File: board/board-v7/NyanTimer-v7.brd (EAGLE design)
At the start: 136.3 x 45 mm, 49 parts, among them IC1 7815DT, IC2 MAX232, IC3 7815DT, SW1 AKIZUKI_SWITCH, U1 328P

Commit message: modified
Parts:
- moved Q1 20.0 mm to (-49.0, -15.0)
- moved C14 10.0 mm to (-68.6, 16.4)
- moved C15 10.0 mm to (-63.5, 16.4)
- moved C12 10.0 mm to (-63.5, 20.2)
- moved C13 10.0 mm to (-68.6, 20.2)
- moved C16 10.0 mm to (-68.6, 12.5)
- moved IC2 10.0 mm to (-66.9, 32.5)
- moved BT1 5.00 mm to (-33.6, 25.8)
- moved BT2 5.00 mm to (33.6, 25.8)
- moved C4 5.00 mm to (-31.2, 21.2)
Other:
- board size 136.3 x 45 mm -> 136 x 45 mm

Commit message: modified
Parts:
- moved C13 139.0 mm to (70.4, 21.2)
- moved IC2 134.0 mm to (67.1, 33.5)
- moved C15 133.9 mm to (70.4, 17.1)
- moved C14 133.1 mm to (64.5, 17.1)
- moved C16 133.1 mm to (64.5, 13.1)
- moved C12 128.0 mm to (64.5, 21.2)
- moved C5 50.0 mm to (-23.0, 5.02)
- moved C6 50.0 mm to (-26.7, 5.04)
- moved PHN1 50.0 mm to (26.7, 2.14)
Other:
- outline, holes or cut-outs redrawn

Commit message: modified
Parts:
- moved C18 89.8 mm to (-1.00, 27.0)
- moved C17 77.6 mm to (-11.0, 27.0)
- moved R12 74.8 mm to (0.00, 20.0)
- moved Q1 63.0 mm to (-6.00, 31.0)
- moved C7 17.7 mm to (19.1, 22.4)
- moved PIN1 17.0 mm to (-30.7, 15.8)
- moved PIN2 17.0 mm to (30.8, 15.9)
- moved C1 12.0 mm to (-19.2, 15.6)
- moved C2 12.0 mm to (19.1, 15.6), turned to 270 degrees
- moved C4 12.0 mm to (-19.2, 21.2)
- moved R10 6.40 mm to (31.1, 8.83), turned to 270 degrees
- moved R11 6.40 mm to (-31.1, 8.84), turned to 270 degrees
- moved R2 5.00 mm to (2.55, 11.1)
- moved R1 5.00 mm to (-2.62, 11.1)
- moved R3 1.00 mm to (-11.4, 11.2)
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
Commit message: modified
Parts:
- C11, C9: value 0.1u -> 2.2u
- C8: value 200u -> 0.1u
- moved C17 12.9 mm to (1.75, 29.2), turned to 90 degrees
- moved R2 5.00 mm to (2.55, 16.1)
- moved R1 5.00 mm to (-2.62, 16.1)
- moved R12 4.00 mm to (0.00, 24.0)
- moved Q1 3.00 mm to (-9.00, 31.0)
- moved C18 2.26 mm to (-1.50, 29.2), turned to 90 degrees
- moved C8 1.50 mm to (5.01, 29.2)
- moved LED1 1.00 mm to (-17.4, 29.0)
- moved LED2 1.00 mm to (17.5, 28.9)
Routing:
- removed copper zone on layer 1, net GND

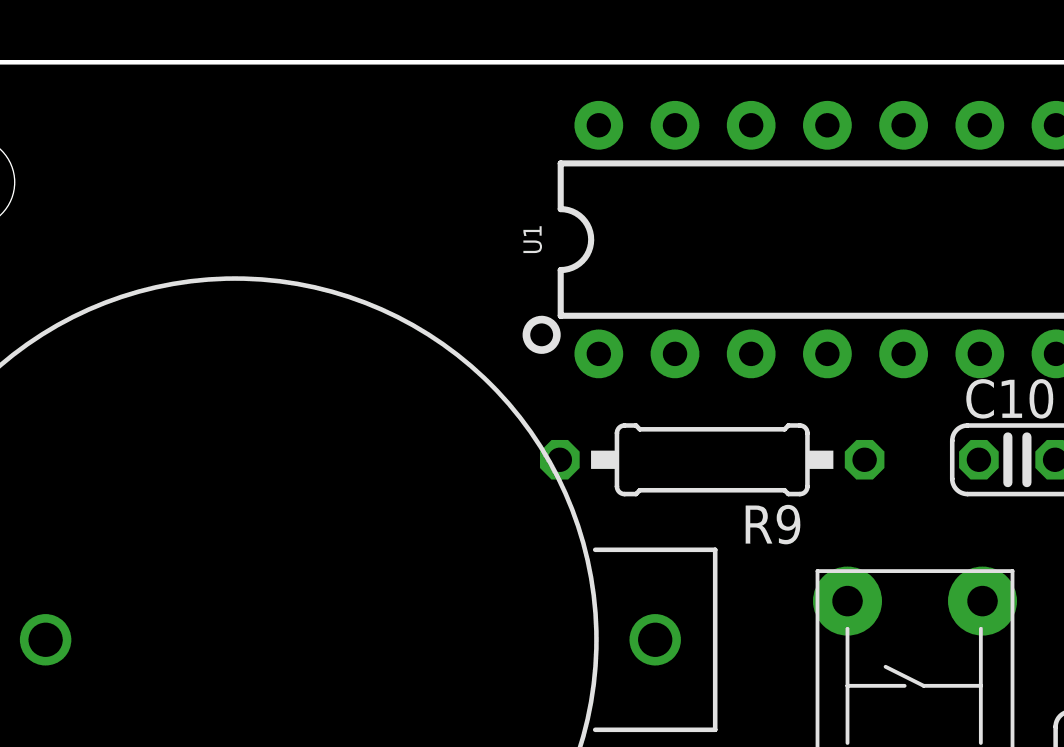
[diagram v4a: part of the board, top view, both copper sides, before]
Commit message: modified padl pin
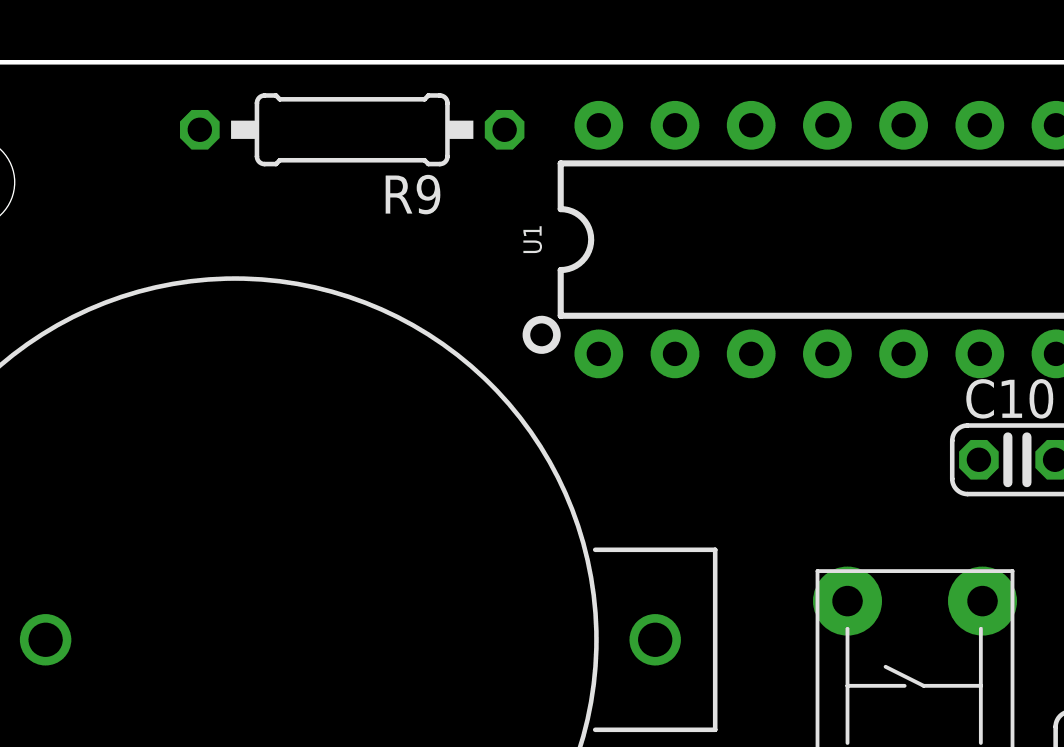
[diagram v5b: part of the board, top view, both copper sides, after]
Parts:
- moved R9 16.3 mm to (-43.8, 42.8)
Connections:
- net PADLIN: now also U1.25; no longer U1.11
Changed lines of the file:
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@@
 <drawing>
 <settings>
-<setting alwaysvectorfont="no"/>
+<setting alwaysvectorfont="yes"/>
 <setting verticaltext="up"/>
 </settings>
@@
 </layers>
 <board>
-<fusionsync huburn="a.cGVyc29uYWw6dWUyZDY1ODA3" projecturn="a.cGVyc29uYWw6dWUyZDY1ODA3IzIwMTgwOTMwMTUxNjc4Mzgx" f3durn="urn:adsk.wipprod:dm.lineage:cDSKwgNKRl2nwQcyNHv1MQ" pcbguid="a41a688f-10bb-486b-9802-a0f971612fa0" lastpulledtime="" lastsyncedchangeguid="592dcdca-8122-b4cd-fe00-eb67763abaf7"/>
+<fusionsync huburn="a.cGVyc29uYWw6dWUyZDY1ODA3" projecturn="a.cGVyc29uYWw6dWUyZDY1ODA3IzIwMTgwOTMwMTUxNjc4Mzgx" f3durn="urn:adsk.wipprod:dm.lineage:3ih9qoiSRh2YeH_9UNAHYQ" pcbguid="ba764a6a-c4ff-48dd-a9cc-70516c013fae" lastpulledtime="" lastsyncedchangeguid="48eea775-bd5d-98d6-e79d-8d9a8075f033"/>
 <plain>
 <hole x="-42" y="4" drill="3"/>
@@
 <element name="BT1" library="akizuki_cr2032" package="AKIZUKI_CR2032" value="AKIZUKI_CR2032" x="-33.65" y="25.75" smashed="yes" rot="R90"/>
 <element name="BT2" library="akizuki_cr2032" package="AKIZUKI_CR2032" value="AKIZUKI_CR2032" x="33.65" y="25.75" smashed="yes" rot="SR270"/>
-<element name="R9" library="resistor" library_urn="urn:adsk.eagle:library:348" package="0207/10" package3d_urn="urn:adsk.eagle:package:23491/2" value="10k" x="-31.75" y="31.75" smashed="yes" rot="R180">
-<attribute name="NAME" x="-28.702" y="30.226" size="1.27" layer="25" ratio="10" rot="R180"/>
-<attribute name="VALUE" x="-29.4894" y="32.385" size="1.27" layer="27" ratio="10" rot="R180"/>
+<element name="R9" library="resistor" library_urn="urn:adsk.eagle:library:348" package="0207/10" package3d_urn="urn:adsk.eagle:package:23491/2" value="10k" x="-43.75" y="42.75" smashed="yes" rot="R180">
+<attribute name="NAME" x="-40.702" y="41.226" size="1.27" layer="25" ratio="10" rot="R180"/>
+<attribute name="VALUE" x="-41.4894" y="43.385" size="1.27" layer="27" ratio="10" rot="R180"/>
 </element>
 <element name="IC2" library="maxim" library_urn="urn:adsk.eagle:library:269" package="DIL16" package3d_urn="urn:adsk.eagle:package:922/2" value="MAX232" x="67.11" y="33.47" smashed="yes" rot="R90">
@@
 <contactref element="C17" pad="2"/>
 <contactref element="C18" pad="2"/>
+<wire x1="53.97" y1="25.75" x2="63.3" y2="27.12" width="0" layer="19" extent="1-1"/>
+<wire x1="69.13" y1="17.15" x2="63.3" y2="27.12" width="0" layer="19" extent="1-1"/>
+<wire x1="65.79" y1="13.14" x2="69.13" y2="17.15" width="0" layer="19" extent="1-1"/>
+<wire x1="32.22" y1="37.16" x2="53.97" y2="25.75" width="0" layer="19" extent="1-1"/>
+<wire x1="17.74" y1="35.56" x2="32.22" y2="37.16" width="0" layer="19" extent="1-1"/>
+<wire x1="18.75" y1="28.91" x2="17.74" y2="35.56" width="0" layer="19" extent="1-1"/>
+<wire x1="11.16" y1="27.94" x2="18.75" y2="28.91" width="0" layer="19" extent="1-1"/>
+<wire x1="8.08" y1="27.9" x2="11.16" y2="27.94" width="0" layer="19" extent="1-1"/>
+<wire x1="5.01" y1="27.92" x2="8.08" y2="27.9" width="0" layer="19" extent="1-1"/>
+<wire x1="1.75" y1="30.47" x2="5.01" y2="27.92" width="0" layer="19" extent="1-1"/>
+<wire x1="-1.5" y1="30.47" x2="1.75" y2="30.47" width="0" layer="19" extent="1-1"/>
+<wire x1="19.14" y1="21.12" x2="18.75" y2="28.91" width="0" layer="19" extent="1-1"/>
+<wire x1="16.53" y1="17.2" x2="19.14" y2="21.12" width="0" layer="19" extent="1-1"/>
+<wire x1="16.53" y1="11.2" x2="16.53" y2="17.2" width="0" layer="19" extent="1-1"/>
+<wire x1="4.07" y1="40.45" x2="1.75" y2="30.47" width="0" layer="19" extent="1-1"/>
+<wire x1="26.69" y1="7.22" x2="16.53" y2="11.2" width="0" layer="19" extent="1-1"/>
+<wire x1="-6.37" y1="17.12" x2="-1.5" y2="30.47" width="0" layer="19" extent="1-1"/>
+<wire x1="-6.37" y1="11.2" x2="-6.37" y2="17.12" width="0" layer="19" extent="1-1"/>
+<wire x1="2.54" y1="2.97" x2="-6.37" y2="11.2" width="0" layer="19" extent="1-1"/>
+<wire x1="-17.75" y1="35.28" x2="-1.5" y2="30.47" width="0" layer="19" extent="1-1"/>
+<wire x1="-20.32" y1="31.75" x2="-17.75" y2="35.28" width="0" layer="19" extent="1-1"/>
+<wire x1="-18.67" y1="29.03" x2="-20.32" y2="31.75" width="0" layer="19" extent="1-1"/>
+<wire x1="-20.29" y1="42.9" x2="-17.75" y2="35.28" width="0" layer="19" extent="1-1"/>
 </signal>
 <signal name="+5V">
@@
 <wire x1="-20.29" y1="35.28" x2="-17.75" y2="42.9" width="0" layer="19" extent="1-1"/>
 <wire x1="-22.86" y1="31.75" x2="-20.29" y2="35.28" width="0" layer="19" extent="1-1"/>
-<wire x1="-26.67" y1="31.75" x2="-22.86" y2="31.75" width="0" layer="19" extent="1-1"/>
-<wire x1="-27.24" y1="27.04" x2="-26.67" y2="31.75" width="0" layer="19" extent="1-1"/>
+<wire x1="-27.24" y1="27.04" x2="-22.86" y2="31.75" width="0" layer="19" extent="1-1"/>
 <wire x1="-27.27" y1="17.98" x2="-27.24" y2="27.04" width="0" layer="19" extent="1-1"/>
 <wire x1="-19.16" y1="19.93" x2="-27.27" y2="17.98" width="0" layer="19" extent="1-1"/>
 <wire x1="-19.18" y1="14.34" x2="-19.16" y2="19.93" width="0" layer="19" extent="1-1"/>
+<wire x1="-38.67" y1="42.75" x2="-22.86" y2="31.75" width="0" layer="19" extent="1-1"/>
 </signal>
 <signal name="BUZ+">
@@
 <contactref element="Q1" pad="2"/>
 <contactref element="C18" pad="1"/>
-<wire x1="-1.5" y1="27.93" x2="-6.587" y2="31" width="0" layer="19" extent="1-1"/>
+<wire x1="-1.5" y1="27.93" x2="5.08" y2="24" width="0" layer="19" extent="1-1"/>
+<wire x1="-6.587" y1="31" x2="-1.5" y2="27.93" width="0" layer="19" extent="1-1"/>
 <wire x1="-12.67" y1="35.28" x2="-6.587" y2="31" width="0" layer="19" extent="1-1"/>
-<wire x1="5.08" y1="24" x2="-1.5" y2="27.93" width="0" layer="19" extent="1-1"/>
 </signal>
 <signal name="VSW">
@@
 <contactref element="R9" pad="2"/>
 <contactref element="U1" pad="1"/>
-<wire x1="-35.53" y1="35.28" x2="-36.83" y2="31.75" width="0" layer="19" extent="1-1"/>
+<wire x1="-35.53" y1="35.28" x2="-48.83" y2="42.75" width="0" layer="19" extent="1-1"/>
 </signal>
 <signal name="VCC">
@@
 <signal name="PADLIN">
 <contactref element="R11" pad="2"/>
-<contactref element="U1" pad="11"/>
-<wire x1="-10.13" y1="35.28" x2="-31.06" y2="3.76" width="0" layer="19" extent="1-1"/>
+<contactref element="U1" pad="25"/>
+<wire x1="-27.91" y1="42.9" x2="-31.06" y2="3.76" width="0" layer="19" extent="1-1"/>
 </signal>
 </signals>

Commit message: modified
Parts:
- moved C7 18.6 mm to (34.1, 11.4)
- moved C1 18.0 mm to (-34.2, 5.61)
- moved C2 18.0 mm to (34.1, 5.61)
- moved C4 18.0 mm to (-34.2, 11.2)
- moved C3 7.07 mm to (30.1, 19.3)
